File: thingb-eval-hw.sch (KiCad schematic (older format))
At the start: 37 parts, among them J1 USB_C_Receptacle_USB2.0, J2 Conn_01x04, J3 Conn_01x04, Q1 S9015, SW1 SW_Push, SW2 SW_Push, SW3 TSWB-3N-CB, U1 ESP32-WROVER, U11 NSI45015WT1G, U2 MCP23008_SO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

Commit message: switch button footprints to be smd switches
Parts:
- SW1, SW2: footprint Button_Switch_THT:SW_PUSH_6mm_H5mm -> Button_Switch_SMD:SW_SPST_EVQPE1
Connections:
- net GND: now also SW1.2; no longer SW1.1
- net at R1.2, U1.3 (EN): now also SW1.1; no longer SW1.2
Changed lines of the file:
@@
 Wire Wire Line
 	1150 4000 1150 3950
-$Comp
-L Switch:SW_Push SW1
-U 1 1 5C9A9A89
-P 850 4250
-F 0 "SW1" H 850 4575 50  0000 C CNN
-F 1 "SW_Push" H 850 4484 50  0000 C CNN
-F 2 "Button_Switch_THT:SW_PUSH_6mm_H5mm" H 850 4250 50  0001 C CNN
-F 3 "~" H 850 4250 50  0001 C CNN
-	1    850  4250
-	1    0    0    -1
-$EndComp
 Wire Wire Line
 	650  4250 600  4250
@@
 F 0 "SW2" H 2900 4925 50  0000 C CNN
 F 1 "SW_Push" H 2900 4834 50  0000 C CNN
-F 2 "Button_Switch_THT:SW_PUSH_6mm_H5mm" H 2900 4600 50  0001 C CNN
+F 2 "Button_Switch_SMD:SW_SPST_EVQPE1" H 2900 4600 50  0001 C CNN
 F 3 "~" H 2900 4600 50  0001 C CNN
 	1    2900 4600
@@
 	1    0    0    -1
 $EndComp
+$Comp
+L Switch:SW_Push SW1
+U 1 1 5C9A9A89
+P 850 4250
+F 0 "SW1" H 850 4575 50  0000 C CNN
+F 1 "SW_Push" H 850 4484 50  0000 C CNN
+F 2 "Button_Switch_SMD:SW_SPST_EVQPE1" H 850 4250 50  0001 C CNN
+F 3 "~" H 850 4250 50  0001 C CNN
+	1    850  4250
+	-1   0    0    -1
+$EndComp
 $EndSCHEMATC

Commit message: add power pins to debugging headers and rename usb nets so that kicad recognizes them as a differential pair
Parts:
- J2: value Conn_01x04 -> Conn_01x06; footprint Connector_PinHeader_2.54mm:PinHeader_1x04_P2.54mm_Vertical -> Connector_PinHeader_2.54mm:PinHeader_1x06_P2.54mm_Vertical; symbol Connector_Generic:Conn_01x04 -> Connector_Generic:Conn_01x06
- J3: value Conn_01x04 -> Conn_01x05; footprint Connector_PinHeader_2.54mm:PinHeader_1x04_P2.54mm_Vertical -> Connector_PinHeader_2.54mm:PinHeader_1x05_P2.54mm_Vertical; symbol Connector_Generic:Conn_01x04 -> Connector_Generic:Conn_01x05
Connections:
- net GND: now also J2.6 (Pin_6), J3.5 (Pin_5)
- net JTAG_MTCK: now also J2.3 (Pin_3); no longer J2.2 (Pin_2)
- net JTAG_MTDI: now also J2.2 (Pin_2); no longer J2.1 (Pin_1)
- net JTAG_MTDO: now also J2.5 (Pin_5); no longer J2.4 (Pin_4)
- net JTAG_MTMS: now also J2.4 (Pin_4); no longer J2.3 (Pin_3)
- net VDD: now also J2.1 (Pin_1)
- net USB_DM renamed USB_D-
- net USB_DP renamed USB_D+
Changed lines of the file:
@@
 NoConn ~ 1550 3000
 Text GLabel 1700 2350 2    39   BiDi ~ 0
-USB_DM
+USB_D-
 Text GLabel 1700 2550 2    39   BiDi ~ 0
-USB_DP
+USB_D+
 Wire Wire Line
 	1650 2550 1700 2550
@@
 	2850 2750 2850 2700
 Text GLabel 2950 2950 0    39   BiDi ~ 0
-USB_DM
+USB_D-
 Text GLabel 2950 2850 0    39   BiDi ~ 0
-USB_DP
+USB_D+
 Wire Wire Line
 	2950 2850 3000 2850
@@
 NoConn ~ 6650 4100
 NoConn ~ 6650 4000
-$Comp
-L Connector_Generic:Conn_01x04 J3
-U 1 1 5D00D675
-P 7950 1050
-F 0 "J3" H 7868 1367 50  0000 C CNN
-F 1 "Conn_01x04" H 7868 1276 50  0000 C CNN
-F 2 "Connector_PinHeader_2.54mm:PinHeader_1x04_P2.54mm_Vertical" H 7950 1050 50  0001 C CNN
-F 3 "~" H 7950 1050 50  0001 C CNN
-	1    7950 1050
-	-1   0    0    -1
-$EndComp
 Wire Wire Line
 	8150 950  8250 950
@@
 Wire Wire Line
 	8850 4350 8850 4850
-Text GLabel 3750 3950 0    39   Output ~ 0
+Text GLabel 3550 4100 0    39   Output ~ 0
 JTAG_MTDO
-Text GLabel 3750 3750 0    39   Input ~ 0
+Text GLabel 3550 3900 0    39   Input ~ 0
 JTAG_MTCK
-Text GLabel 3750 3850 0    39   Input ~ 0
+Text GLabel 3550 4000 0    39   Input ~ 0
 JTAG_MTMS
-Text GLabel 3750 3650 0    39   Input ~ 0
+Text GLabel 3550 3800 0    39   Input ~ 0
 JTAG_MTDI
 Wire Wire Line
-	3750 3950 3800 3950
-Wire Wire Line
-	3800 3850 3750 3850
-Wire Wire Line
-	3750 3750 3800 3750
-Wire Wire Line
-	3750 3650 3800 3650
-$Comp
-L Connector_Generic:Conn_01x04 J2
+	3550 4100 3600 4100
+Wire Wire Line
+	3600 4000 3550 4000
+Wire Wire Line
+	3550 3900 3600 3900
+Wire Wire Line
+	3550 3800 3600 3800
+$Comp
+L Connector_Generic:Conn_01x06 J2
 U 1 1 5D4CA230
-P 4000 3750
-F 0 "J2" H 3918 4067 50  0000 C CNN
-F 1 "Conn_01x04" H 3918 3976 50  0000 C CNN
-F 2 "Connector_PinHeader_2.54mm:PinHeader_1x04_P2.54mm_Vertical" H 4000 3750 50  0001 C CNN
-F 3 "~" H 4000 3750 50  0001 C CNN
-	1    4000 3750
+P 3800 3900
+F 0 "J2" H 4100 3950 50  0000 C CNN
+F 1 "Conn_01x06" H 4100 3850 50  0000 C CNN
+F 2 "Connector_PinHeader_2.54mm:PinHeader_1x06_P2.54mm_Vertical" H 3800 3900 50  0001 C CNN
+F 3 "~" H 3800 3900 50  0001 C CNN
+	1    3800 3900
 	1    0    0    -1
 $EndComp
@@
 	-1   0    0    -1
 $EndComp
+$Comp
+L Connector_Generic:Conn_01x05 J3
+U 1 1 5D00D675
+P 7950 1150
+F 0 "J3" H 8250 1200 50  0000 C CNN
+F 1 "Conn_01x05" H 8250 1100 50  0000 C CNN
+F 2 "Connector_PinHeader_2.54mm:PinHeader_1x05_P2.54mm_Vertical" H 7950 1150 50  0001 C CNN
+F 3 "~" H 7950 1150 50  0001 C CNN
+	1    7950 1150
+	-1   0    0    -1
+$EndComp
+$Comp
+L power:GND #PWR0101
+U 1 1 5DC175EF
+P 8250 1400
+F 0 "#PWR0101" H 8250 1150 50  0001 C CNN
+F 1 "GND" H 8255 1227 50  0000 C CNN
+F 2 "" H 8250 1400 50  0001 C CNN
+F 3 "" H 8250 1400 50  0001 C CNN
+	1    8250 1400
+	1    0    0    -1
+$EndComp
+Wire Wire Line
+	8150 1350 8250 1350
+Wire Wire Line
+	8250 1350 8250 1400
+$Comp
+L power:GND #PWR0102
+U 1 1 5DC8B84C
+P 3550 4250
+F 0 "#PWR0102" H 3550 4000 50  0001 C CNN
+F 1 "GND" H 3555 4077 50  0000 C CNN
+F 2 "" H 3550 4250 50  0001 C CNN
+F 3 "" H 3550 4250 50  0001 C CNN
+	1    3550 4250
+	1    0    0    -1
+$EndComp
+Wire Wire Line
+	3600 4200 3550 4200
+Wire Wire Line
+	3550 4200 3550 4250
+$Comp
+L power:VDD #PWR0103
+U 1 1 5DCA34FE
+P 3550 3650
+F 0 "#PWR0103" H 3550 3500 50  0001 C CNN
+F 1 "VDD" H 3567 3823 50  0000 C CNN
+F 2 "" H 3550 3650 50  0001 C CNN
+F 3 "" H 3550 3650 50  0001 C CNN
+	1    3550 3650
+	1    0    0    -1
+$EndComp
+Wire Wire Line
+	3600 3700 3550 3700
+Wire Wire Line
+	3550 3700 3550 3650
 $EndSCHEMATC

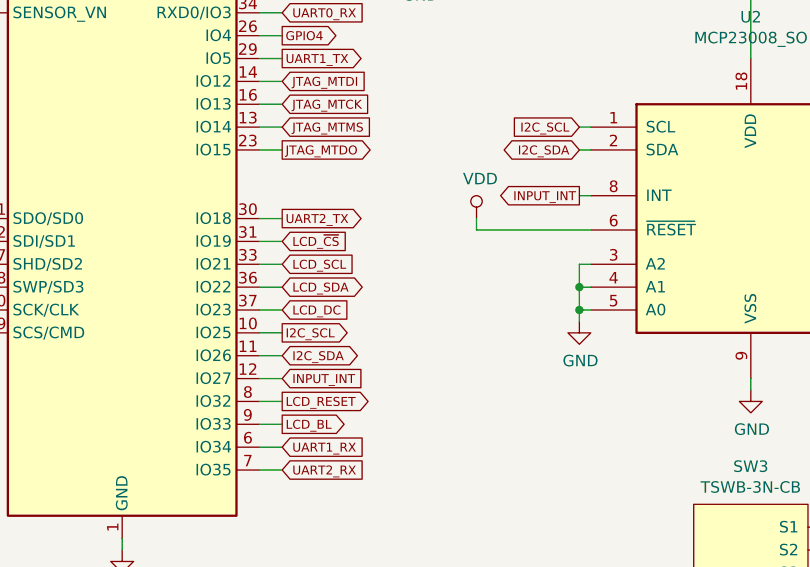
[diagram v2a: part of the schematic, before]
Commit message: i am dumb and forgot pullups on the i2c lines
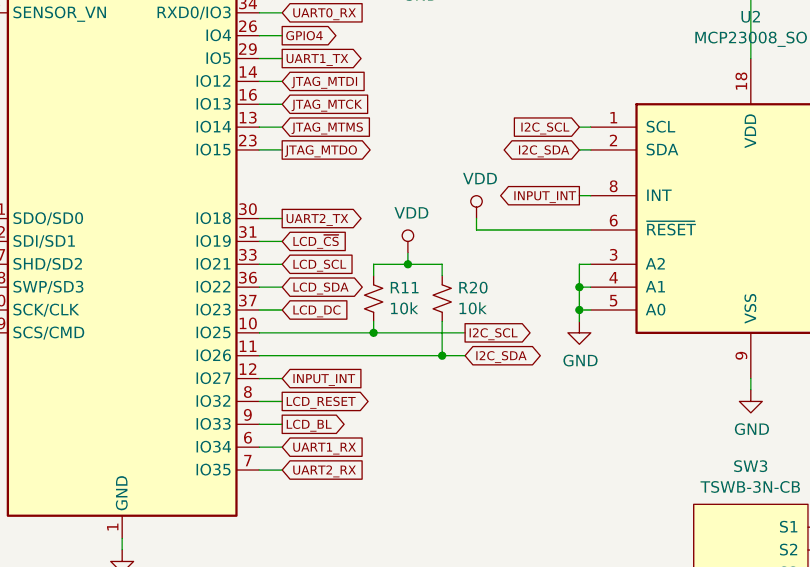
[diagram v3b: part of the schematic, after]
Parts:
- added R11, R20: 10k, Resistor_SMD:R_0603_1608Metric_Pad1.05x0.95mm_HandSolder, symbol Device:R_Small_US
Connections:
- net I2C_SCL: now also R11.2
- net I2C_SDA: now also R20.2
- net VDD: now also R11.1, R20.1
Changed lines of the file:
@@
 	2450 6500 2550 6500
 Wire Wire Line
-	2550 6400 2450 6400
-Wire Wire Line
-	2450 6300 2550 6300
+	3350 6400 3250 6400
+Wire Wire Line
+	2450 6300 2950 6300
 Wire Wire Line
 	2450 6200 2550 6200
@@
 Text GLabel 3850 5500 0    39   BiDi ~ 0
 I2C_SDA
-Text GLabel 2550 6300 2    39   Output ~ 0
+Text GLabel 3350 6300 2    39   Output ~ 0
 I2C_SCL
-Text GLabel 2550 6400 2    39   BiDi ~ 0
+Text GLabel 3350 6400 2    39   BiDi ~ 0
 I2C_SDA
 $Comp
@@
 Wire Wire Line
 	3550 3700 3550 3650
+$Comp
+L Device:R_Small_US R11
+U 1 1 5DDBAE04
+P 2950 6150
+F 0 "R11" H 3018 6196 50  0000 L CNN
+F 1 "10k" H 3018 6105 50  0000 L CNN
+F 2 "Resistor_SMD:R_0603_1608Metric_Pad1.05x0.95mm_HandSolder" H 2950 6150 50  0001 C CNN
+F 3 "~" H 2950 6150 50  0001 C CNN
+	1    2950 6150
+	1    0    0    -1
+$EndComp
+Wire Wire Line
+	2950 6300 2950 6250
+Connection ~ 2950 6300
+Wire Wire Line
+	2950 6300 3350 6300
+$Comp
+L power:VDD #PWR052
+U 1 1 5DE02908
+P 3100 5950
+F 0 "#PWR052" H 3100 5800 50  0001 C CNN
+F 1 "VDD" H 3117 6123 50  0000 C CNN
+F 2 "" H 3100 5950 50  0001 C CNN
+F 3 "" H 3100 5950 50  0001 C CNN
+	1    3100 5950
+	1    0    0    -1
+$EndComp
+Wire Wire Line
+	2950 6050 2950 6000
+$Comp
+L Device:R_Small_US R20
+U 1 1 5DE1B8D1
+P 3250 6150
+F 0 "R20" H 3318 6196 50  0000 L CNN
+F 1 "10k" H 3318 6105 50  0000 L CNN
+F 2 "Resistor_SMD:R_0603_1608Metric_Pad1.05x0.95mm_HandSolder" H 3250 6150 50  0001 C CNN
+F 3 "~" H 3250 6150 50  0001 C CNN
+	1    3250 6150
+	1    0    0    -1
+$EndComp
+Wire Wire Line
+	3250 6400 3250 6250
+Connection ~ 3250 6400
+Wire Wire Line
+	3250 6400 2450 6400
+Wire Wire Line
+	2950 6000 3100 6000
+Wire Wire Line
+	3250 6000 3250 6050
+Wire Wire Line
+	3100 6000 3100 5950
+Connection ~ 3100 6000
+Wire Wire Line
+	3100 6000 3250 6000
 $EndSCHEMATC
